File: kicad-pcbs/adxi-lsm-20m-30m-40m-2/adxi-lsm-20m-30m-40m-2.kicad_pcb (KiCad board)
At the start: 2 copper layers, 126.3 x 71.1 mm, 122 parts, among them J1 ANT, J2 PA-DRAIN, J3 PA-SUPPLY, J4 C1-GND

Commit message: Final board
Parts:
- removed L10, L12, L13, L14, L15, L16, L17, L18, L19, L20, L21, L5, L6, L7, L73, L74, L75, L8, L9: 6.8uH, Inductor_SMD:L_0805_2012Metric
- removed L27, L28, L29, L30, L31, L32, L33, L34, L35, L36, L37, L38, L39, L40, L41, L42, L43, L44, L45, L46, L47, L48, L49, L50, L51, L52, L53, L54, L55, L56, L57: 470nH, Inductor_SMD:L_1008_2520Metric
- removed L76: 5.6uH, Inductor_SMD:L_0805_2012Metric
- removed L86, L87, L89: 680nH, Inductor_SMD:L_0603_1608Metric
- removed L91: 2.2uH, adxi-footprints:L_Chilisin_NLC252018-2.92x2.50x2.20
- added L11: 2.2uH, Inductor_SMD:L_0603_1608Metric, F.Cu at (121.2, 102.5)
- added L23: 2.2uH, Inductor_SMD:L_0603_1608Metric, F.Cu at (116.0, 104.1)
- added L24: 680nH, Inductor_SMD:L_0603_1608Metric, F.Cu at (116.2, 108.2)
- added L58: 680nH, Inductor_SMD:L_0603_1608Metric, F.Cu at (121.2, 106.2)
- added L59: 680nH, Inductor_SMD:L_0603_1608Metric, F.Cu at (117.8, 106.1)
- added L60: 680nH, Inductor_SMD:L_0603_1608Metric, F.Cu at (104.7, 91.7)
- added L61: 680nH, Inductor_SMD:L_0603_1608Metric, F.Cu at (102.9, 92.8)
- added L62: 680nH, Inductor_SMD:L_0603_1608Metric, F.Cu at (106.6, 91.6)
- added L63: 680nH, Inductor_SMD:L_0603_1608Metric, F.Cu at (108.6, 92.9)
- added L64: 680nH, Inductor_SMD:L_0603_1608Metric, F.Cu at (119.2, 93.7)
- added L65: 680nH, Inductor_SMD:L_0603_1608Metric, F.Cu at (119.6, 108.2)
- added L66: 680nH, Inductor_SMD:L_0603_1608Metric, F.Cu at (116.5, 92.7)
- added L67: 680nH, Inductor_SMD:L_0603_1608Metric, F.Cu at (121.7, 92.7)
- added L68: 680nH, Inductor_SMD:L_0603_1608Metric, F.Cu at (119.1, 91.8)
- added L69: 2.2uH, Inductor_SMD:L_0603_1608Metric, F.Cu at (119.4, 104.3)
- added L70: 2.2uH, Inductor_SMD:L_0603_1608Metric, F.Cu at (117.8, 102.5)
- L25, L26: value 470nH -> 3.9uH; footprint Inductor_SMD:L_1008_2520Metric -> Inductor_SMD:L_1812_4532Metric
- L3, L4: value 6.8uH -> 22uH; footprint Inductor_SMD:L_0805_2012Metric -> Inductor_SMD:L_Sunlord_SWPA3015S
- moved JP28 24.2 mm to (147.3, 93.3)
- moved JP26 24.2 mm to (150.2, 100.0)
- moved C11 24.2 mm to (148.4, 97.0)
- moved C14 24.2 mm to (144.9, 100.5)
- moved C30 24.2 mm to (146.1, 99.3)
- moved C7 24.2 mm to (147.2, 98.2)
- moved JP27 24.2 mm to (152.1, 98.0)
- moved JP29 24.2 mm to (145.4, 95.3)
- moved JP30 24.2 mm to (143.4, 97.2)
- moved C29 24.2 mm to (148.8, 95.0)
- moved C35 24.2 mm to (150.6, 95.5)
- moved JP20 24.2 mm to (148.2, 101.9)
- moved L26 12.8 mm to (162.1, 106.9), turned to 137 degrees
- moved L3 12.5 mm to (132.6, 123.3)
- moved C20 9.06 mm to (101.8, 90.2), turned to 180 degrees
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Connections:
- L26 pad 2: Net-(L26-Pad2) -> Net-(JP20-B)
- L3 pad 1: Net-(L12-Pad1) -> Net-(C12-Pad2)
- L85 pad 1: Net-(L10-Pad2) -> Net-(L4-Pad2)
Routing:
- net Net-(L10-Pad2): track 63.1 -> 0.00 mm
- net Net-(JP20-B): track 66.5 -> 43.8 mm
- net Net-(L3-Pad2): track 3.20 -> 24.5 mm
- net Net-(L4-Pad2): track 3.03 -> 23.5 mm
- net /GND: track 134.1 -> 153.1 mm
- net Net-(L12-Pad1): track 17.1 -> 0.00 mm
- net Net-(C12-Pad2): track 5.45 -> 17.6 mm
- net Net-(C38-Pad1): track 19.8 -> 30.3 mm
- net Net-(J3-Pin_1): track 55.0 -> 61.9 mm
- net Net-(L61-Pad2): track 0.00 -> 5.76 mm
- net Net-(C20-Pad1): track 13.2 -> 7.72 mm
- net Net-(L36-Pad2): track 4.19 -> 0.00 mm
- net Net-(L13-Pad2): track 3.76 -> 0.00 mm
- net Net-(L5-Pad2): track 3.74 -> 0.00 mm
- net Net-(L17-Pad2): track 3.70 -> 0.00 mm
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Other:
- board text removed: "SRF=170MHZ I>3A 7.755μH 0.594Ω"

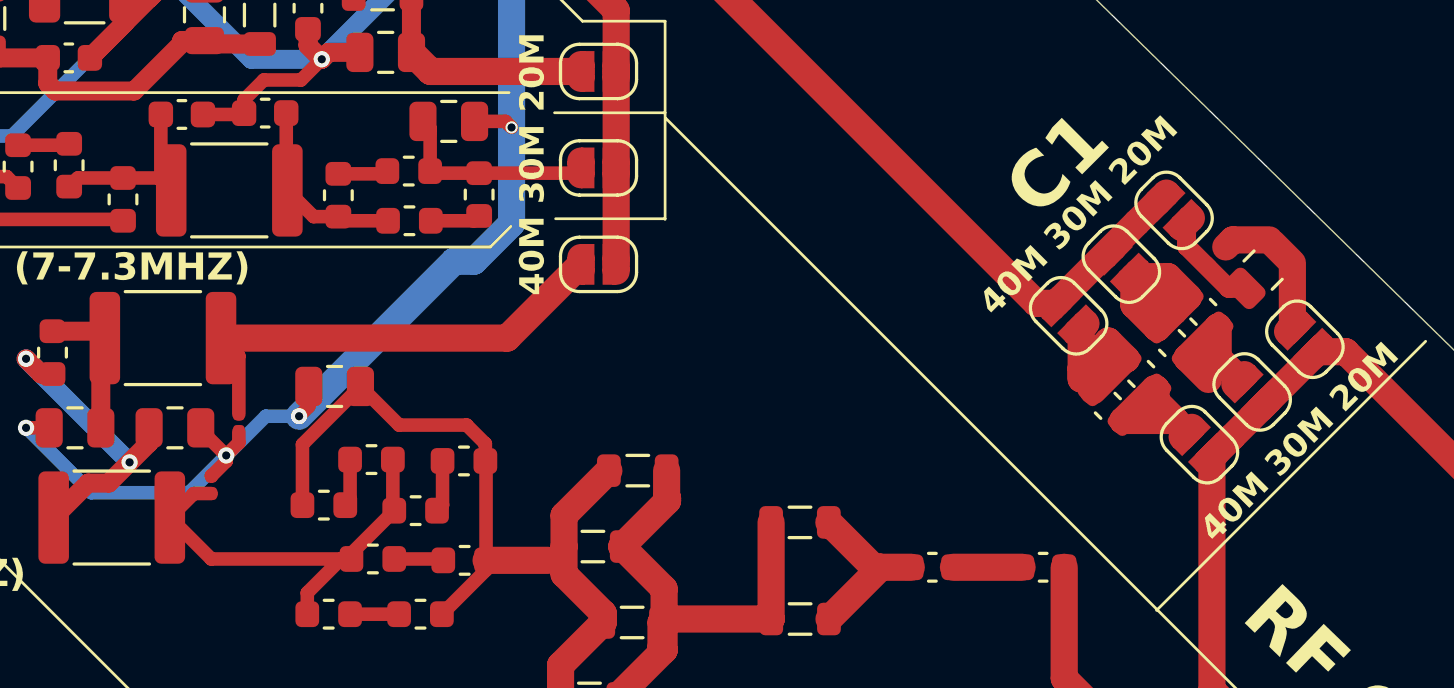
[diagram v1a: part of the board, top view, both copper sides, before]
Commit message: Fix 150pF 0603 footprint incorrectly specified as 0201
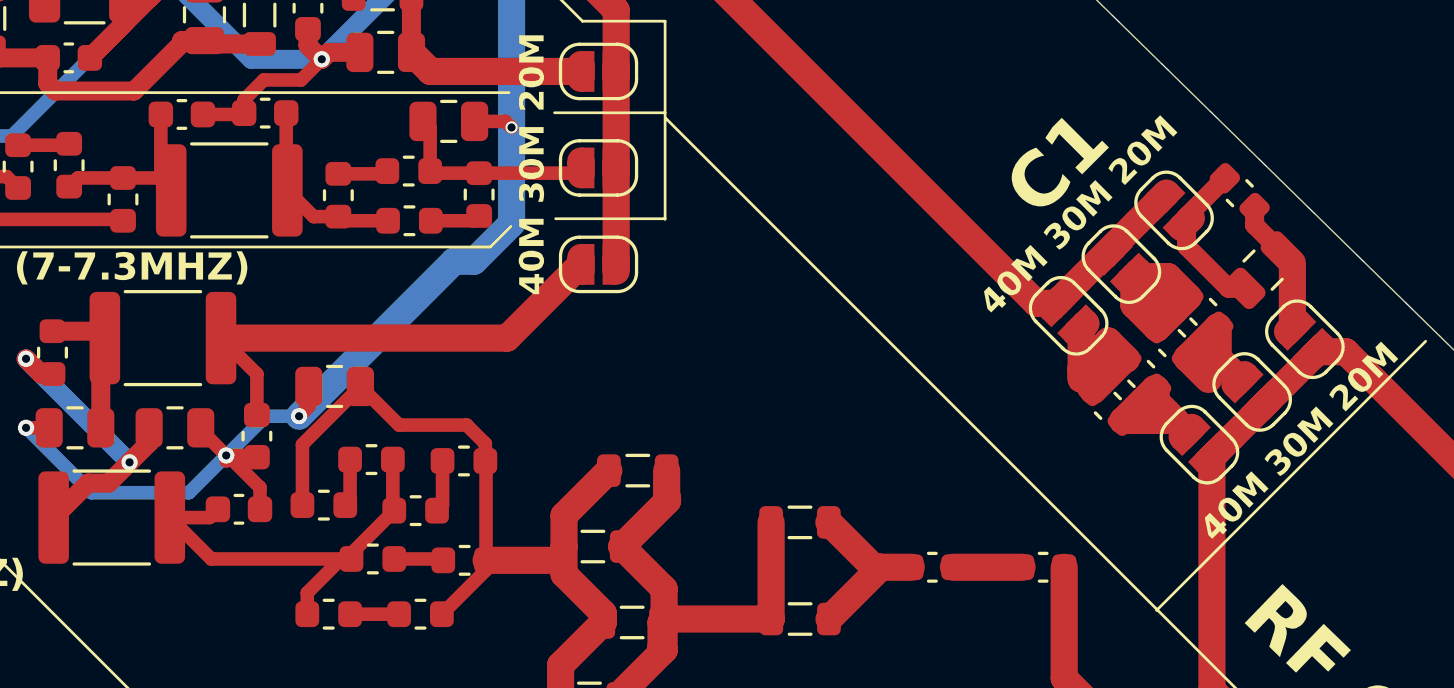
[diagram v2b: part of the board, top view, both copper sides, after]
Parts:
- C29, C41, C42: footprint Capacitor_SMD:C_0201_0603Metric -> Capacitor_SMD:C_0603_1608Metric
- moved C29 2.54 mm to (149.7, 92.7), turned to 135 degrees
- moved C41 1.36 mm to (112.9, 104.3), turned to 0 degrees
- moved C42 0.83 mm to (113.5, 101.6)
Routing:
- net Net-(JP28-B): track 3.65 -> 5.87 mm
- net /GND: track 153.1 -> 154.9 mm
